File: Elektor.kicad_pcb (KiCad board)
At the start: 2 copper layers, 50 x 40 mm, 56 parts, among them J1 Conn_Coaxial, J13 Conn_Coaxial, J6 Conn_01x03_Pin, J8 Conn_01x02, Q1 BF545B, U1 Si5351A-B-GT, U2 74HC04, U3 74HC4066D_653, U5 MCP6022, U6 AUDIOSHIELD-REVD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

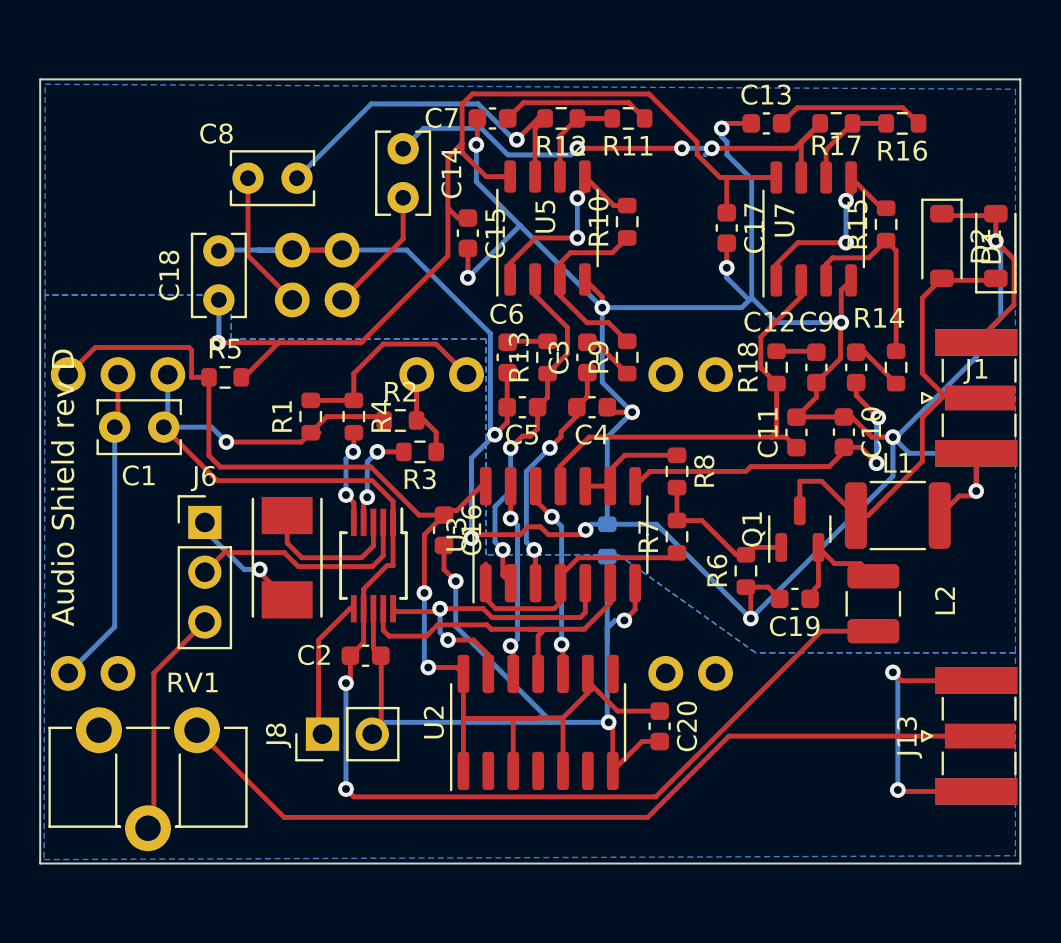
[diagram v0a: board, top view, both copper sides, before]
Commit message: amelioration liaison des 2 masses
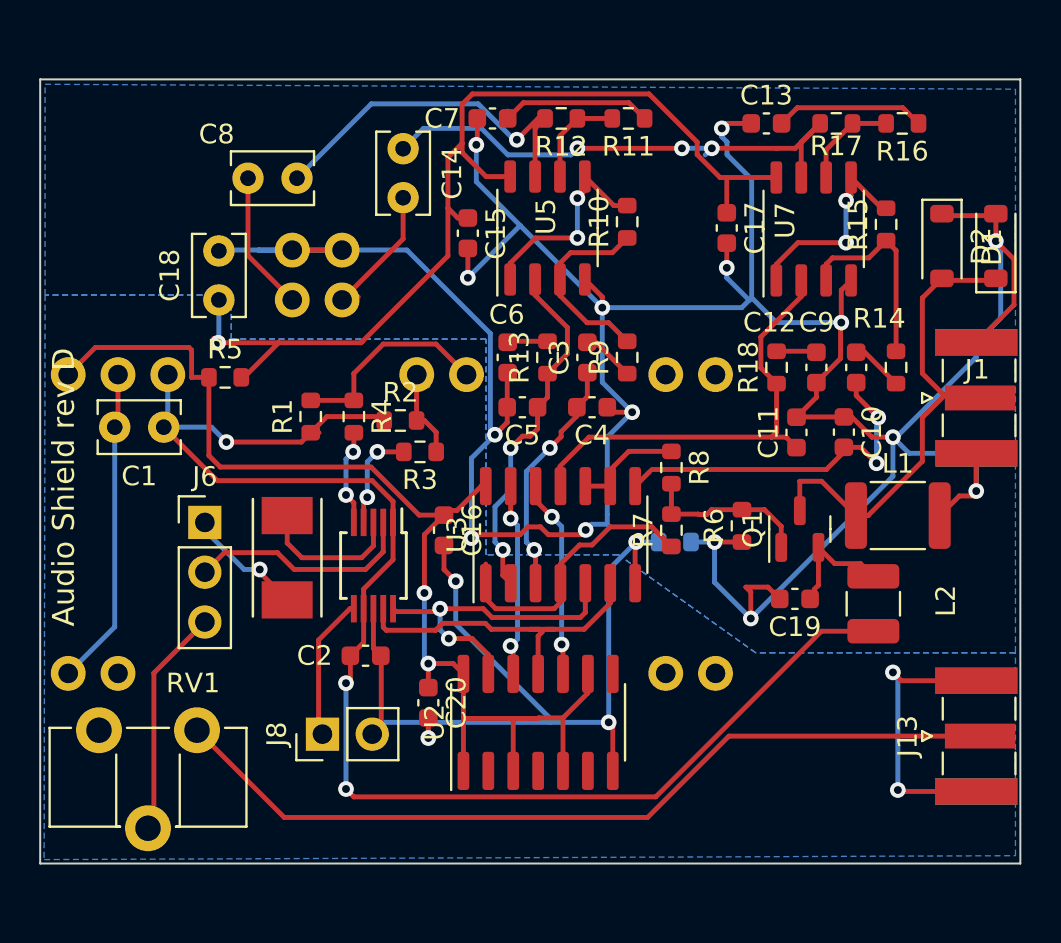
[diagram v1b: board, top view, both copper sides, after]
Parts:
- moved C20 11.9 mm to (176.8, 92.8)
- moved R19 3.45 mm to (189.4, 84.6), turned to 0 degrees
- moved R6 2.31 mm to (192.8, 83.8)
- moved R7 0.43 mm to (189.2, 84.0)
- moved R8 0.35 mm to (189.2, 80.8)
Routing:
- net Net-(U2G-VCC): track 63.1 -> 59.9 mm
- net GNDA: track 176.7 -> 174.7 mm, vias 14 -> 15
- net Net-(U3-1Y): track 13.7 -> 14.7 mm
- net Net-(Q1-S): track 7.87 -> 8.69 mm
- net Net-(U3-3Z): track 6.21 -> 5.61 mm
- net GND: track 81.4 -> 80.9 mm, vias 5 -> 6

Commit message: SMA generateur externe à gauche
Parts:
- moved J13 45.6 mm to (159.2, 96.8), turned to -90 degrees
- moved J8 3.49 mm to (174.6, 93.0), turned to 0 degrees
- moved RV1 1.28 mm to (164.2, 93.2), turned to 0 degrees
- moved U2 0.72 mm to (183.0, 94.2)
- moved C20 0.60 mm to (177.4, 92.8)
- moved J6 0.52 mm to (165.8, 83.3)
- moved C2 0.45 mm to (173.8, 90.0)
- moved Y1 0.28 mm to (169.8, 85.6)
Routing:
- net Net-(J13-In): track 44.6 -> 7.17 mm
- net GND: track 80.9 -> 87.0 mm, vias 6 -> 5
- net Net-(J6-Pin_3): track 11.7 -> 8.75 mm
- net Net-(U2G-VCC): track 59.9 -> 61.7 mm
- net Net-(J8-Pin_1): track 7.35 -> 9.02 mm
- net 3.3V: track 75.6 -> 77.0 mm
- net Net-(U1-CLK0): track 16.8 -> 17.5 mm
- net Net-(U3-4E): track 10.2 -> 10.8 mm

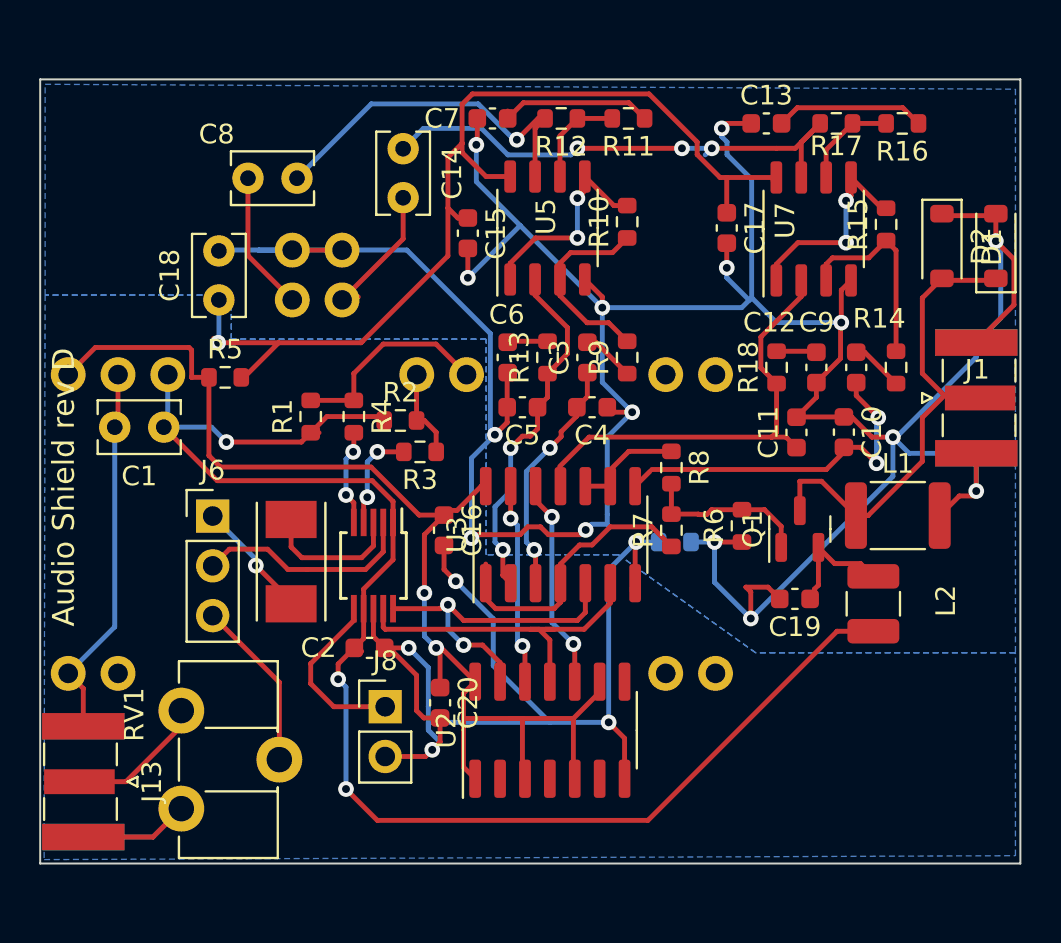
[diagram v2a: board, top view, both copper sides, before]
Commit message: decouplages, capa de liaison generateur externe, marges de prehension, trous de fixations
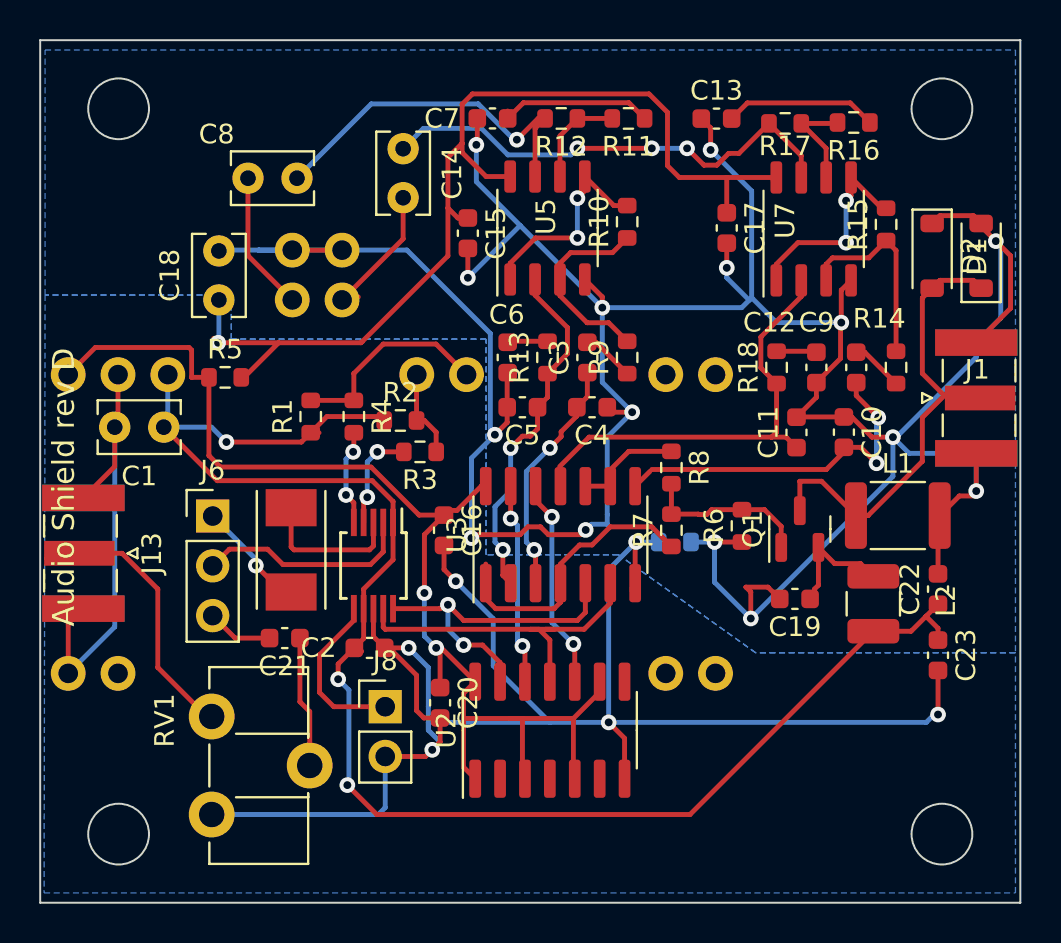
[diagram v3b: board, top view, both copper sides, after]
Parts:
- added C21: 100n, Capacitor_SMD:C_0603_1608Metric, F.Cu at (169.5, 89.5)
- added C22: 100n, Capacitor_SMD:C_0603_1608Metric, F.Cu at (202.8, 87.0)
- added C23: 100n, Capacitor_SMD:C_0603_1608Metric, F.Cu at (202.8, 90.4)
- moved J13 11.7 mm to (159.2, 85.2)
- moved R17 2.61 mm to (195.0, 63.2)
- moved C13 2.56 mm to (191.5, 63.0)
- moved R16 2.48 mm to (198.5, 63.2)
- moved RV1 1.58 mm to (165.8, 93.5)
- moved D1 0.90 mm to (205.0, 70.0)
- moved D2 0.71 mm to (202.5, 70.0)
- moved Y1 0.60 mm to (169.8, 85.0)
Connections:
- RV1 pad 2: Net-(J6-Pin_3) -> Net-(C21-Pad1)
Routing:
- net GND: track 87.0 -> 111.5 mm, vias 5 -> 6
- net Net-(C21-Pad1): track 0.00 -> 6.71 mm
- net Net-(J13-In): track 7.17 -> 12.3 mm
- net 3.3V: track 77.0 -> 82.0 mm
- net Net-(J6-Pin_3): track 8.75 -> 3.93 mm
- net Net-(C14-Pad1): track 26.6 -> 24.5 mm
- net GNDA: track 174.7 -> 176.7 mm
- net 5VA: track 51.8 -> 53.1 mm
- net Net-(D1-K): track 25.0 -> 24.3 mm
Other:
- board size 50 x 40 mm -> 50 x 44 mm

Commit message: marquage
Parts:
- moved C11 0.33 mm to (195.2, 79.0)
- moved L2 0.25 mm to (199.2, 87.8)
- moved C16 0.10 mm to (177.7, 84.0)
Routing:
- net Net-(U3-4Y): track 22.2 -> 23.0 mm
- net Net-(U2G-VCC): track 61.7 -> 61.2 mm
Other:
- board text added: "SDR TEENSY F1FGV F1VL"
